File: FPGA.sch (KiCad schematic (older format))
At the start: 1 part, among them U300 LFE5U

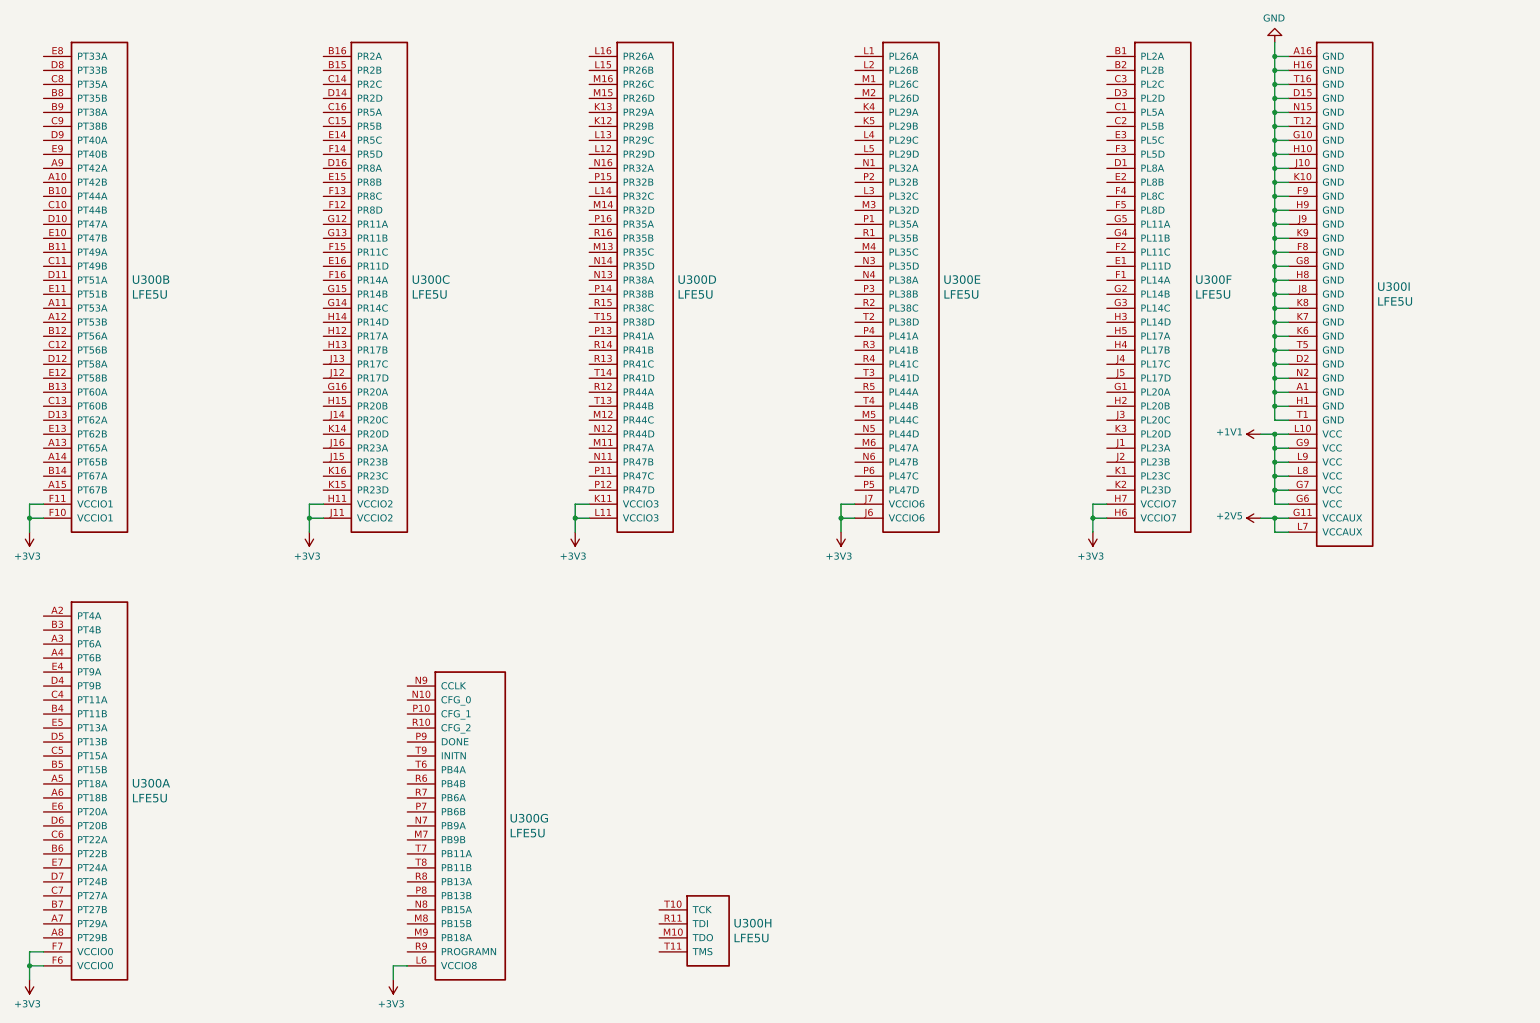
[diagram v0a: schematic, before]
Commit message: use LFE5U-12F-8BG256C schematic symbol
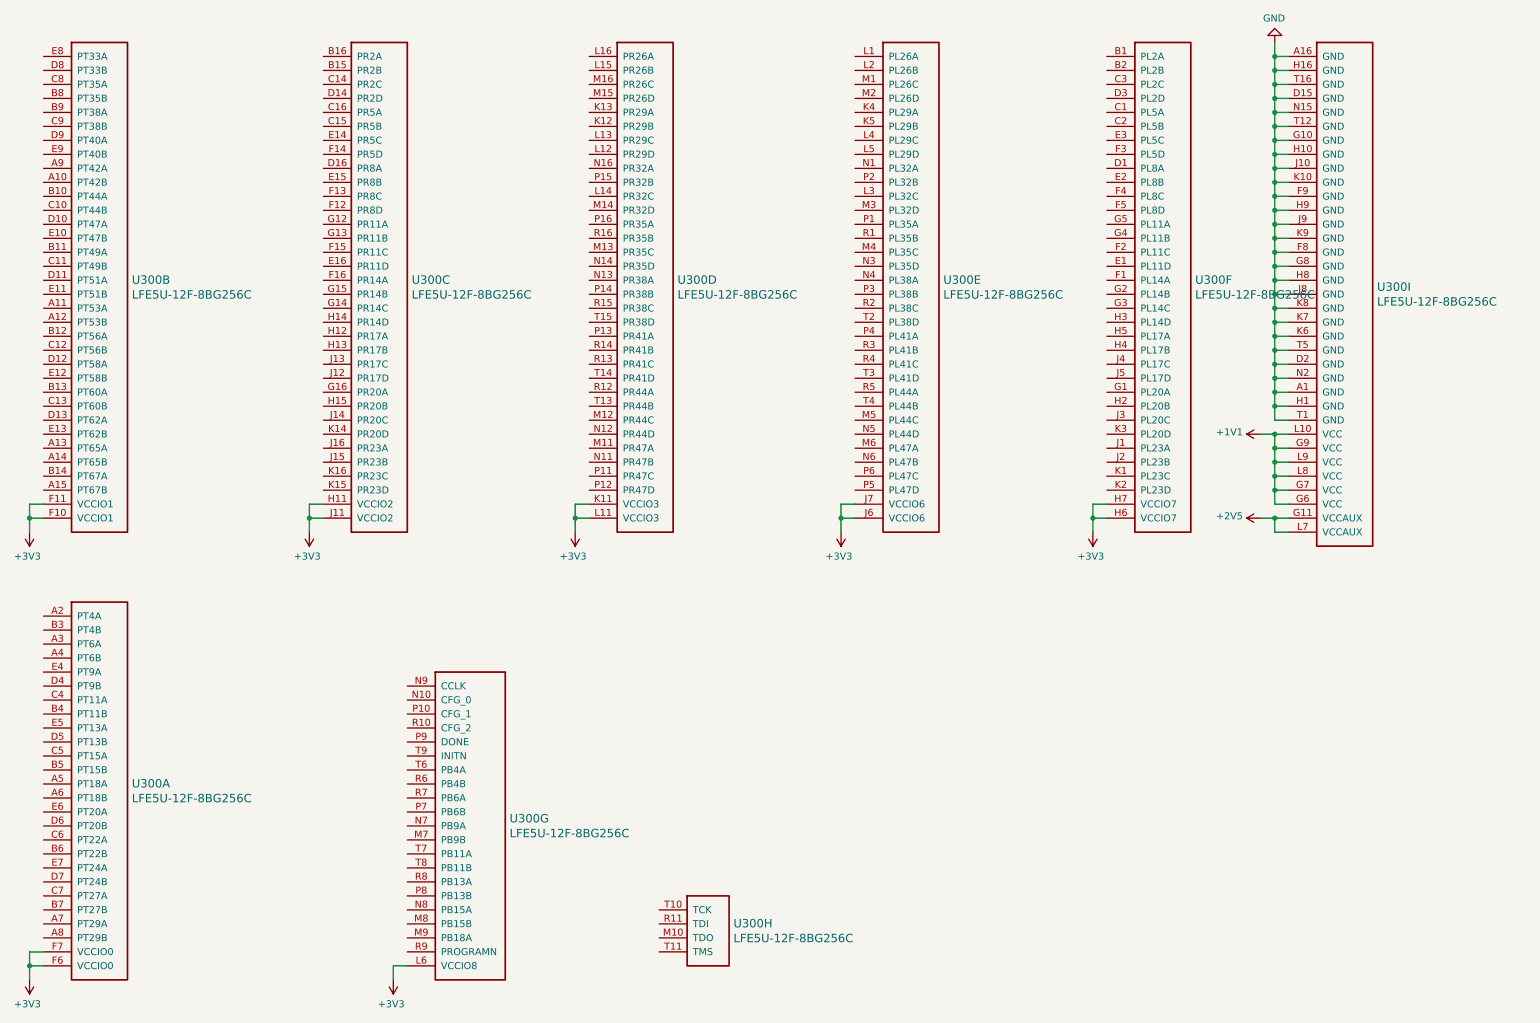
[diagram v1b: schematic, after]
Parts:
- removed U300: LFE5U, Package_BGA:BGA-256_14.0x14.0mm_Layout16x16_P0.8mm_Ball0.45mm_Pad0.32mm_NSMD, symbol kipart:LFE5U
- added U300: LFE5U-12F-8BG256C, Package_BGA:BGA-256_14.0x14.0mm_Layout16x16_P0.8mm_Ball0.45mm_Pad0.32mm_NSMD, symbol ecp5:LFE5U-12F-8BG256C
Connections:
- net +1V1: now also U300.G6 (VCC), U300.G7 (VCC), U300.G9 (VCC), U300.L10 (VCC), U300.L8 (VCC), U300.L9 (VCC)
- net +2V5: now also U300.G11 (VCCAUX), U300.L7 (VCCAUX)
- net +3V3: now also U300.F10 (VCCIO1), U300.F11 (VCCIO1), U300.F6 (VCCIO0), U300.F7 (VCCIO0), U300.H11 (VCCIO2), U300.H6 (VCCIO7), U300.H7 (VCCIO7), U300.J11 (VCCIO2), U300.J6 (VCCIO6), U300.J7 (VCCIO6), U300.K11 (VCCIO3), U300.L11 (VCCIO3), U300.L6 (VCCIO8)
- net GND: now also U300.A1 (GND), U300.A16 (GND), U300.D15 (GND), U300.D2 (GND), U300.F8 (GND), U300.F9 (GND), U300.G10 (GND), U300.G8 (GND), U300.H1 (GND), U300.H10 (GND), U300.H16 (GND), U300.H8 (GND), U300.H9 (GND), U300.J10 (GND), U300.J8 (GND), U300.J9 (GND), U300.K10 (GND), U300.K6 (GND), U300.K7 (GND), U300.K8 (GND), U300.K9 (GND), U300.N15 (GND), U300.N2 (GND), U300.T1 (GND), U300.T12 (GND), U300.T16 (GND), U300.T5 (GND)
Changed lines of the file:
@@
 $EndDescr
 $Comp
-L kipart:LFE5U U300
-U 1 1 5C27FE45
-P 1400 4900
-F 0 "U300" H 2031 3703 60  0000 L CNN
-F 1 "LFE5U" H 2031 3597 60  0000 L CNN
-F 2 "Package_BGA:BGA-256_14.0x14.0mm_Layout16x16_P0.8mm_Ball0.45mm_Pad0.32mm_NSMD" H 1600 4950 60  0001 L CNN
-F 3 "" H 1400 4900 50  0001 C CNN
-	1    1400 4900
-	1    0    0    -1
-$EndComp
-$Comp
-L kipart:LFE5U U300
-U 2 1 5C27FED4
-P 1400 900
-F 0 "U300" H 2031 -697 60  0000 L CNN
-F 1 "LFE5U" H 2031 -803 60  0000 L CNN
-F 2 "Package_BGA:BGA-256_14.0x14.0mm_Layout16x16_P0.8mm_Ball0.45mm_Pad0.32mm_NSMD" H 1600 950 60  0001 L CNN
-F 3 "" H 1400 900 50  0001 C CNN
-	2    1400 900
-	1    0    0    -1
-$EndComp
-$Comp
-L kipart:LFE5U U300
-U 3 1 5C27FF3F
-P 3400 900
-F 0 "U300" H 4031 -697 60  0000 L CNN
-F 1 "LFE5U" H 4031 -803 60  0000 L CNN
-F 2 "Package_BGA:BGA-256_14.0x14.0mm_Layout16x16_P0.8mm_Ball0.45mm_Pad0.32mm_NSMD" H 3600 950 60  0001 L CNN
-F 3 "" H 3400 900 50  0001 C CNN
-	3    3400 900
-	1    0    0    -1
-$EndComp
-$Comp
-L kipart:LFE5U U300
-U 4 1 5C27FF9B
-P 5300 900
-F 0 "U300" H 5931 -697 60  0000 L CNN
-F 1 "LFE5U" H 5931 -803 60  0000 L CNN
-F 2 "Package_BGA:BGA-256_14.0x14.0mm_Layout16x16_P0.8mm_Ball0.45mm_Pad0.32mm_NSMD" H 5500 950 60  0001 L CNN
-F 3 "" H 5300 900 50  0001 C CNN
-	4    5300 900
-	1    0    0    -1
-$EndComp
-$Comp
-L kipart:LFE5U U300
-U 5 1 5C280000
-P 7200 900
-F 0 "U300" H 7831 -697 60  0000 L CNN
-F 1 "LFE5U" H 7831 -803 60  0000 L CNN
-F 2 "Package_BGA:BGA-256_14.0x14.0mm_Layout16x16_P0.8mm_Ball0.45mm_Pad0.32mm_NSMD" H 7400 950 60  0001 L CNN
-F 3 "" H 7200 900 50  0001 C CNN
-	5    7200 900
-	1    0    0    -1
-$EndComp
-$Comp
-L kipart:LFE5U U300
-U 6 1 5C28008A
-P 9000 900
-F 0 "U300" H 9631 -697 60  0000 L CNN
-F 1 "LFE5U" H 9631 -803 60  0000 L CNN
-F 2 "Package_BGA:BGA-256_14.0x14.0mm_Layout16x16_P0.8mm_Ball0.45mm_Pad0.32mm_NSMD" H 9200 950 60  0001 L CNN
-F 3 "" H 9000 900 50  0001 C CNN
-	6    9000 900
-	1    0    0    -1
-$EndComp
-$Comp
-L kipart:LFE5U U300
-U 7 1 5C28012F
-P 4000 5400
-F 0 "U300" H 4731 4453 60  0000 L CNN
-F 1 "LFE5U" H 4731 4347 60  0000 L CNN
-F 2 "Package_BGA:BGA-256_14.0x14.0mm_Layout16x16_P0.8mm_Ball0.45mm_Pad0.32mm_NSMD" H 4200 5450 60  0001 L CNN
-F 3 "" H 4000 5400 50  0001 C CNN
-	7    4000 5400
-	1    0    0    -1
-$EndComp
-$Comp
-L kipart:LFE5U U300
-U 8 1 5C28023C
-P 5800 7000
-F 0 "U300" H 6331 6903 60  0000 L CNN
-F 1 "LFE5U" H 6331 6797 60  0000 L CNN
-F 2 "Package_BGA:BGA-256_14.0x14.0mm_Layout16x16_P0.8mm_Ball0.45mm_Pad0.32mm_NSMD" H 6000 7050 60  0001 L CNN
-F 3 "" H 5800 7000 50  0001 C CNN
-	8    5800 7000
-	1    0    0    -1
-$EndComp
-$Comp
-L kipart:LFE5U U300
-U 9 1 5C280315
-P 10300 900
-F 0 "U300" H 10931 -747 60  0000 L CNN
-F 1 "LFE5U" H 10931 -853 60  0000 L CNN
-F 2 "Package_BGA:BGA-256_14.0x14.0mm_Layout16x16_P0.8mm_Ball0.45mm_Pad0.32mm_NSMD" H 10500 950 60  0001 L CNN
-F 3 "" H 10300 900 50  0001 C CNN
-	9    10300 900
-	1    0    0    -1
-$EndComp
-$Comp
-L power:GND #PWR?
+L power:GND #PWR0113
 U 1 1 5C2849DC
 P 10200 800
-F 0 "#PWR?" H 10200 550 50  0001 C CNN
+F 0 "#PWR0113" H 10200 550 50  0001 C CNN
 F 1 "GND" H 10205 627 50  0000 C CNN
 F 2 "" H 10200 800 50  0001 C CNN
@@
 	10200 4300 10200 4200
 $Comp
-L power:+1V1 #PWR?
+L power:+1V1 #PWR0114
 U 1 1 5C286DFF
 P 10100 3600
-F 0 "#PWR?" H 10100 3450 50  0001 C CNN
+F 0 "#PWR0114" H 10100 3450 50  0001 C CNN
 F 1 "+1V1" V 10115 3728 50  0000 L CNN
 F 2 "" H 10100 3600 50  0001 C CNN
@@
 $EndComp
 $Comp
-L power:+2V5 #PWR?
+L power:+2V5 #PWR0115
 U 1 1 5C286E81
 P 10100 4200
-F 0 "#PWR?" H 10100 4050 50  0001 C CNN
+F 0 "#PWR0115" H 10100 4050 50  0001 C CNN
 F 1 "+2V5" V 10115 4328 50  0000 L CNN
 F 2 "" H 10100 4200 50  0001 C CNN
@@
 Connection ~ 10200 3600
 $Comp
-L power:+3V3 #PWR?
+L power:+3V3 #PWR0116
 U 1 1 5C288CB6
 P 8900 4300
-F 0 "#PWR?" H 8900 4150 50  0001 C CNN
+F 0 "#PWR0116" H 8900 4150 50  0001 C CNN
 F 1 "+3V3" H 8915 4473 50  0000 C CNN
 F 2 "" H 8900 4300 50  0001 C CNN
@@
 	8900 4200 8900 4300
 $Comp
-L power:+3V3 #PWR?
+L power:+3V3 #PWR0117
 U 1 1 5C28AEB8
 P 7100 4300
-F 0 "#PWR?" H 7100 4150 50  0001 C CNN
+F 0 "#PWR0117" H 7100 4150 50  0001 C CNN
 F 1 "+3V3" H 7115 4473 50  0000 C CNN
 F 2 "" H 7100 4300 50  0001 C CNN
@@
 	7100 4200 7100 4300
 $Comp
-L power:+3V3 #PWR?
+L power:+3V3 #PWR0118
 U 1 1 5C28C4AD
 P 5200 4300
-F 0 "#PWR?" H 5200 4150 50  0001 C CNN
+F 0 "#PWR0118" H 5200 4150 50  0001 C CNN
 F 1 "+3V3" H 5215 4473 50  0000 C CNN
 F 2 "" H 5200 4300 50  0001 C CNN
@@
 	5200 4200 5200 4300
 $Comp
-L power:+3V3 #PWR?
+L power:+3V3 #PWR0119
 U 1 1 5C28DDFC
 P 3300 4300
-F 0 "#PWR?" H 3300 4150 50  0001 C CNN
+F 0 "#PWR0119" H 3300 4150 50  0001 C CNN
 F 1 "+3V3" H 3315 4473 50  0000 C CNN
 F 2 "" H 3300 4300 50  0001 C CNN
@@
 	3300 4200 3300 4300
 $Comp
-L power:+3V3 #PWR?
+L power:+3V3 #PWR0120
 U 1 1 5C28FB65
 P 1300 4300
-F 0 "#PWR?" H 1300 4150 50  0001 C CNN
+F 0 "#PWR0120" H 1300 4150 50  0001 C CNN
 F 1 "+3V3" H 1315 4473 50  0000 C CNN
 F 2 "" H 1300 4300 50  0001 C CNN
@@
 	1300 4200 1300 4300
 $Comp
-L power:+3V3 #PWR?
+L power:+3V3 #PWR0121
 U 1 1 5C291CE2
 P 1300 7500
-F 0 "#PWR?" H 1300 7350 50  0001 C CNN
+F 0 "#PWR0121" H 1300 7350 50  0001 C CNN
 F 1 "+3V3" H 1315 7673 50  0000 C CNN
 F 2 "" H 1300 7500 50  0001 C CNN
@@
 	1300 7400 1300 7500
 $Comp
-L power:+3V3 #PWR?
+L power:+3V3 #PWR0122
 U 1 1 5C294279
 P 3900 7500
-F 0 "#PWR?" H 3900 7350 50  0001 C CNN
+F 0 "#PWR0122" H 3900 7350 50  0001 C CNN
 F 1 "+3V3" H 3915 7673 50  0000 C CNN
 F 2 "" H 3900 7500 50  0001 C CNN
@@
 Wire Wire Line
 	3900 7400 3900 7500
+$Comp
+L ecp5:LFE5U-12F-8BG256C U300
+U 1 1 5C294BF5
+P 1400 4900
+F 0 "U300" H 2031 3703 60  0000 L CNN
+F 1 "LFE5U-12F-8BG256C" H 2031 3597 60  0000 L CNN
+F 2 "Package_BGA:BGA-256_14.0x14.0mm_Layout16x16_P0.8mm_Ball0.45mm_Pad0.32mm_NSMD" H 1600 4950 60  0001 L CNN
+F 3 "" H 1400 4900 50  0001 C CNN
+	1    1400 4900
+	1    0    0    -1
+$EndComp
+$Comp
+L ecp5:LFE5U-12F-8BG256C U300
+U 2 1 5C294CF4
+P 1400 900
+F 0 "U300" H 2031 -697 60  0000 L CNN
+F 1 "LFE5U-12F-8BG256C" H 2031 -803 60  0000 L CNN
+F 2 "Package_BGA:BGA-256_14.0x14.0mm_Layout16x16_P0.8mm_Ball0.45mm_Pad0.32mm_NSMD" H 1600 950 60  0001 L CNN
+F 3 "" H 1400 900 50  0001 C CNN
+	2    1400 900
+	1    0    0    -1
+$EndComp
+$Comp
+L ecp5:LFE5U-12F-8BG256C U300
+U 3 1 5C294D6A
+P 3400 900
+F 0 "U300" H 4031 -697 60  0000 L CNN
+F 1 "LFE5U-12F-8BG256C" H 4031 -803 60  0000 L CNN
+F 2 "Package_BGA:BGA-256_14.0x14.0mm_Layout16x16_P0.8mm_Ball0.45mm_Pad0.32mm_NSMD" H 3600 950 60  0001 L CNN
+F 3 "" H 3400 900 50  0001 C CNN
+	3    3400 900
+	1    0    0    -1
+$EndComp
+$Comp
+L ecp5:LFE5U-12F-8BG256C U300
+U 4 1 5C294DF3
+P 5300 900
+F 0 "U300" H 5931 -697 60  0000 L CNN
+F 1 "LFE5U-12F-8BG256C" H 5931 -803 60  0000 L CNN
+F 2 "Package_BGA:BGA-256_14.0x14.0mm_Layout16x16_P0.8mm_Ball0.45mm_Pad0.32mm_NSMD" H 5500 950 60  0001 L CNN
+F 3 "" H 5300 900 50  0001 C CNN
+	4    5300 900
+	1    0    0    -1
+$EndComp
+$Comp
+L ecp5:LFE5U-12F-8BG256C U300
+U 5 1 5C294E89
+P 7200 900
+F 0 "U300" H 7831 -697 60  0000 L CNN
+F 1 "LFE5U-12F-8BG256C" H 7831 -803 60  0000 L CNN
+F 2 "Package_BGA:BGA-256_14.0x14.0mm_Layout16x16_P0.8mm_Ball0.45mm_Pad0.32mm_NSMD" H 7400 950 60  0001 L CNN
+F 3 "" H 7200 900 50  0001 C CNN
+	5    7200 900
+	1    0    0    -1
+$EndComp
+$Comp
+L ecp5:LFE5U-12F-8BG256C U300
+U 6 1 5C294F92
+P 9000 900
+F 0 "U300" H 9631 -697 60  0000 L CNN
+F 1 "LFE5U-12F-8BG256C" H 9631 -803 60  0000 L CNN
+F 2 "Package_BGA:BGA-256_14.0x14.0mm_Layout16x16_P0.8mm_Ball0.45mm_Pad0.32mm_NSMD" H 9200 950 60  0001 L CNN
+F 3 "" H 9000 900 50  0001 C CNN
+	6    9000 900
+	1    0    0    -1
+$EndComp
+$Comp
+L ecp5:LFE5U-12F-8BG256C U300
+U 7 1 5C294FEE
+P 4000 5400
+F 0 "U300" H 4731 4453 60  0000 L CNN
+F 1 "LFE5U-12F-8BG256C" H 4731 4347 60  0000 L CNN
+F 2 "Package_BGA:BGA-256_14.0x14.0mm_Layout16x16_P0.8mm_Ball0.45mm_Pad0.32mm_NSMD" H 4200 5450 60  0001 L CNN
+F 3 "" H 4000 5400 50  0001 C CNN
+	7    4000 5400
+	1    0    0    -1
+$EndComp
+$Comp
+L ecp5:LFE5U-12F-8BG256C U300
+U 8 1 5C29504D
+P 5800 7000
+F 0 "U300" H 6331 6903 60  0000 L CNN
+F 1 "LFE5U-12F-8BG256C" H 6331 6797 60  0000 L CNN
+F 2 "Package_BGA:BGA-256_14.0x14.0mm_Layout16x16_P0.8mm_Ball0.45mm_Pad0.32mm_NSMD" H 6000 7050 60  0001 L CNN
+F 3 "" H 5800 7000 50  0001 C CNN
+	8    5800 7000
+	1    0    0    -1
+$EndComp
+$Comp
+L ecp5:LFE5U-12F-8BG256C U300
+U 9 1 5C2950ED
+P 10300 900
+F 0 "U300" H 10931 -747 60  0000 L CNN
+F 1 "LFE5U-12F-8BG256C" H 10931 -853 60  0000 L CNN
+F 2 "Package_BGA:BGA-256_14.0x14.0mm_Layout16x16_P0.8mm_Ball0.45mm_Pad0.32mm_NSMD" H 10500 950 60  0001 L CNN
+F 3 "" H 10300 900 50  0001 C CNN
+	9    10300 900
+	1    0    0    -1
+$EndComp
 $EndSCHEMATC
